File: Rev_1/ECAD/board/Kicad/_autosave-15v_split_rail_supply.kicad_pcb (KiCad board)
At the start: 2 copper layers, 18 parts, among them Q1 IPP029N15NM6, U1 LM3478MA

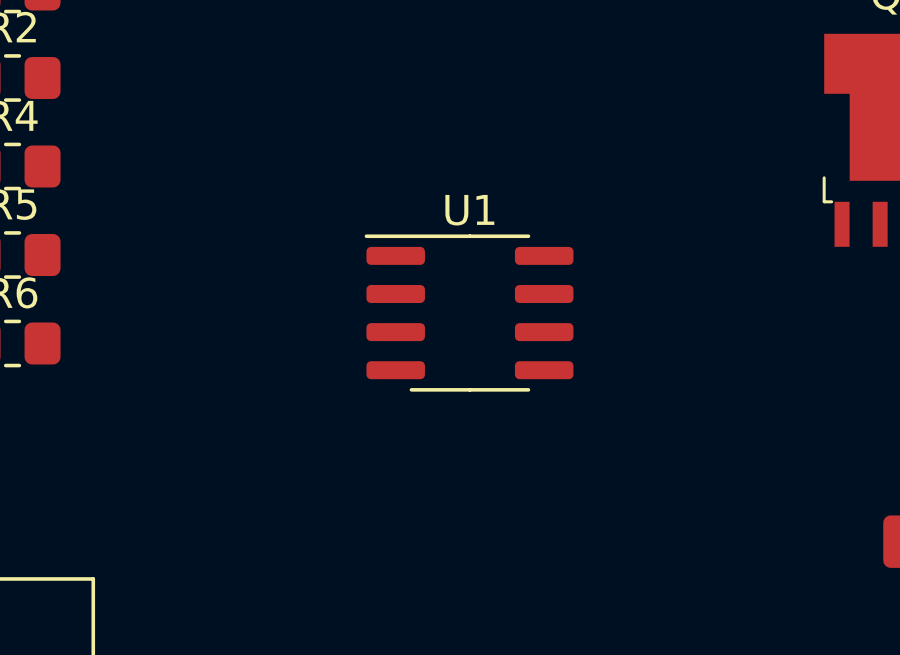
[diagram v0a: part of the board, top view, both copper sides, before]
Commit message: Assigned footprint and 3d-models for +17V switch regulator
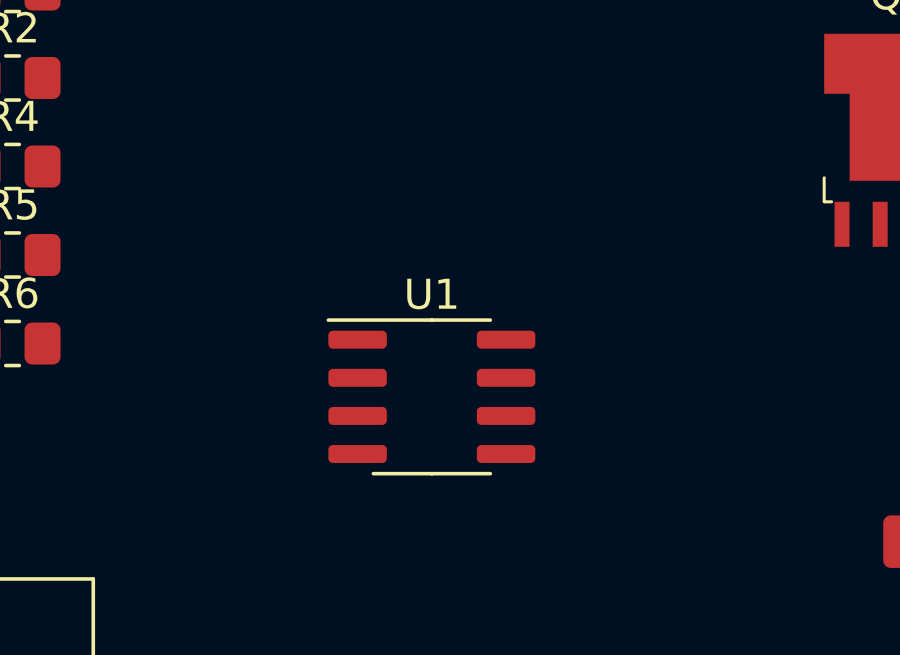
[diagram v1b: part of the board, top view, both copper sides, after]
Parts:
- moved U1 3.07 mm to (76.7, 51.8)
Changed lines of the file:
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@@
   )
   (footprint "Package_SO:SOIC-8_3.9x4.9mm_P1.27mm" (layer "F.Cu")
-    (at 77.978 49.022)
+    (at 76.708 51.816)
     (descr "SOIC, 8 Pin (JEDEC MS-012AA, https://www.analog.com/media/en/package-pcb-resources/package/pkg_pdf/soic_narrow-r/r_8.pdf), generated with kicad-footprint-generator ipc_gullwing_generator.py")
     (tags "SOIC SO")
